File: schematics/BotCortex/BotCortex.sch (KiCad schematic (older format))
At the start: 60 parts, among them P1 2x Serial, P10 Stepper Upperarm, P11 Stepper Hip, P12 POWER_IN, P13 PowerEnableIn, P14 Power Stepper 2, P15 Power Stepper 3, P16 Power Stepper 4, P17 PowerEnableOut, P18 Power Stepper 5, P19 ODroid Power, P2 Herkulex Servo, P20 POTI 10K, P21 Reset_Conn, P22 Reset Conn, P23 LED-Driver-I2C, P24 UART6, P25 Thermal_Printer, P28 Power Stepper 1, P3 Encoder Socket 0, P4 Encoder Socket, P5 Stepper Elbow, P6 Power In uC Servo 9V, P7 Power Out uC Servo, P8 Stepper Forearm, P9 Stepper Wrist, Q1 BC237, Q2 BC237, SW2 reset, U1 7805, U2 LM7809ACT, U3 LM7809ACT, U4 Teensy_3.5, U5 7803

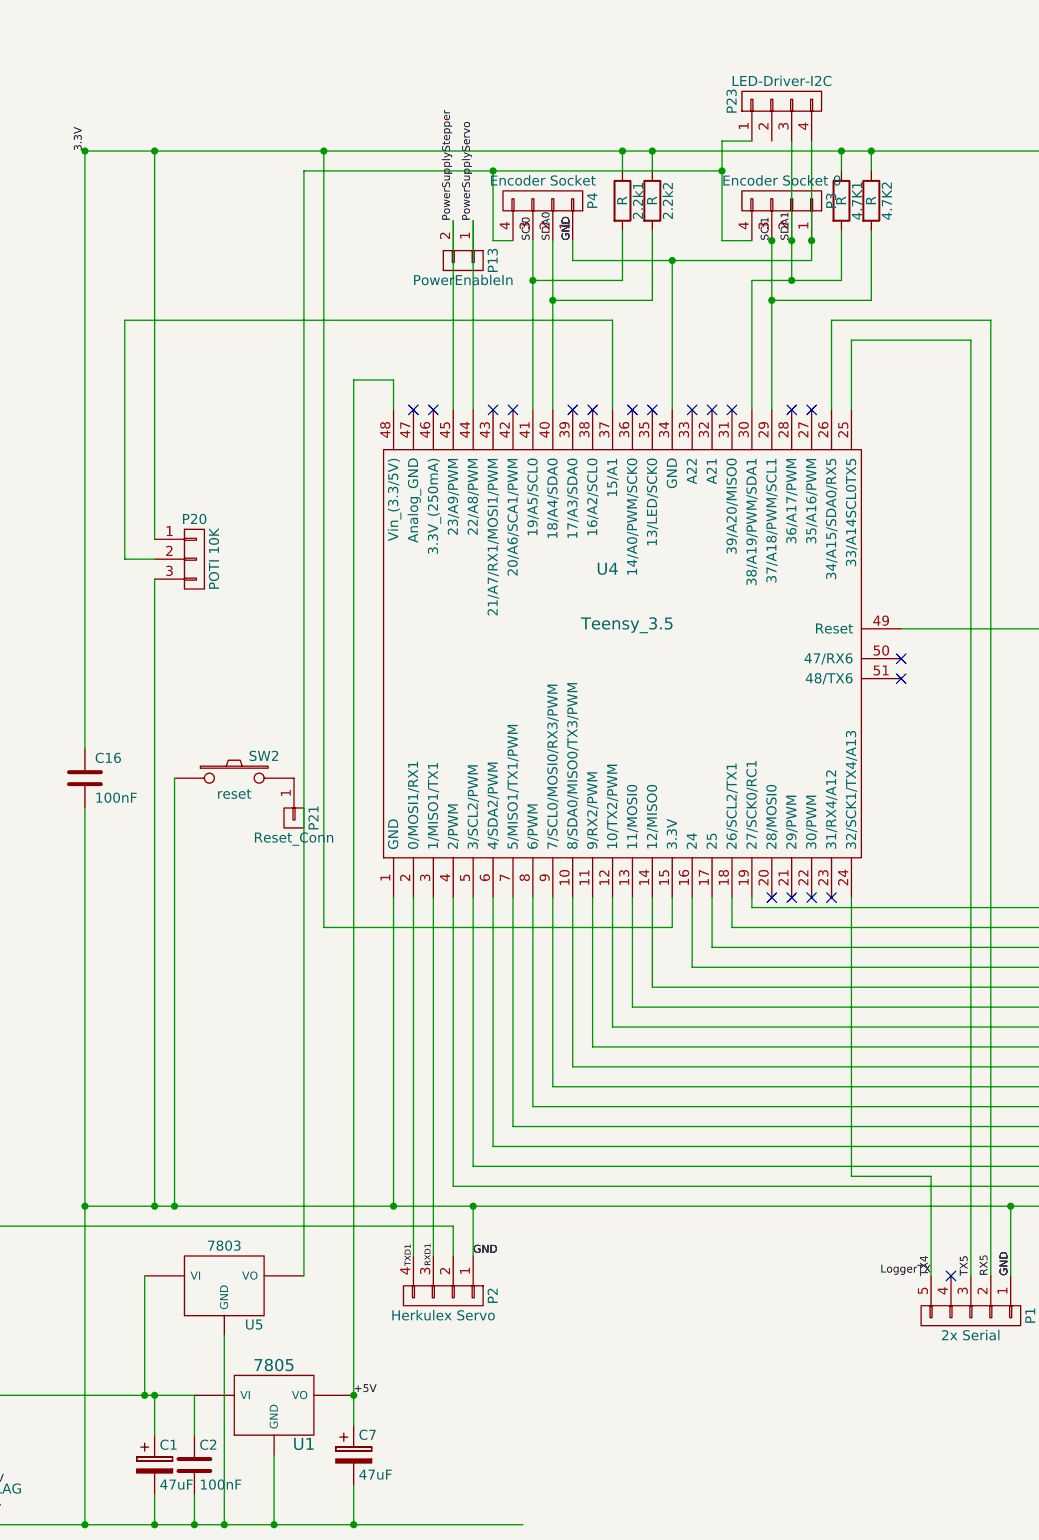
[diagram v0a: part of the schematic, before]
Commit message: encoder und stepper work with tinsy
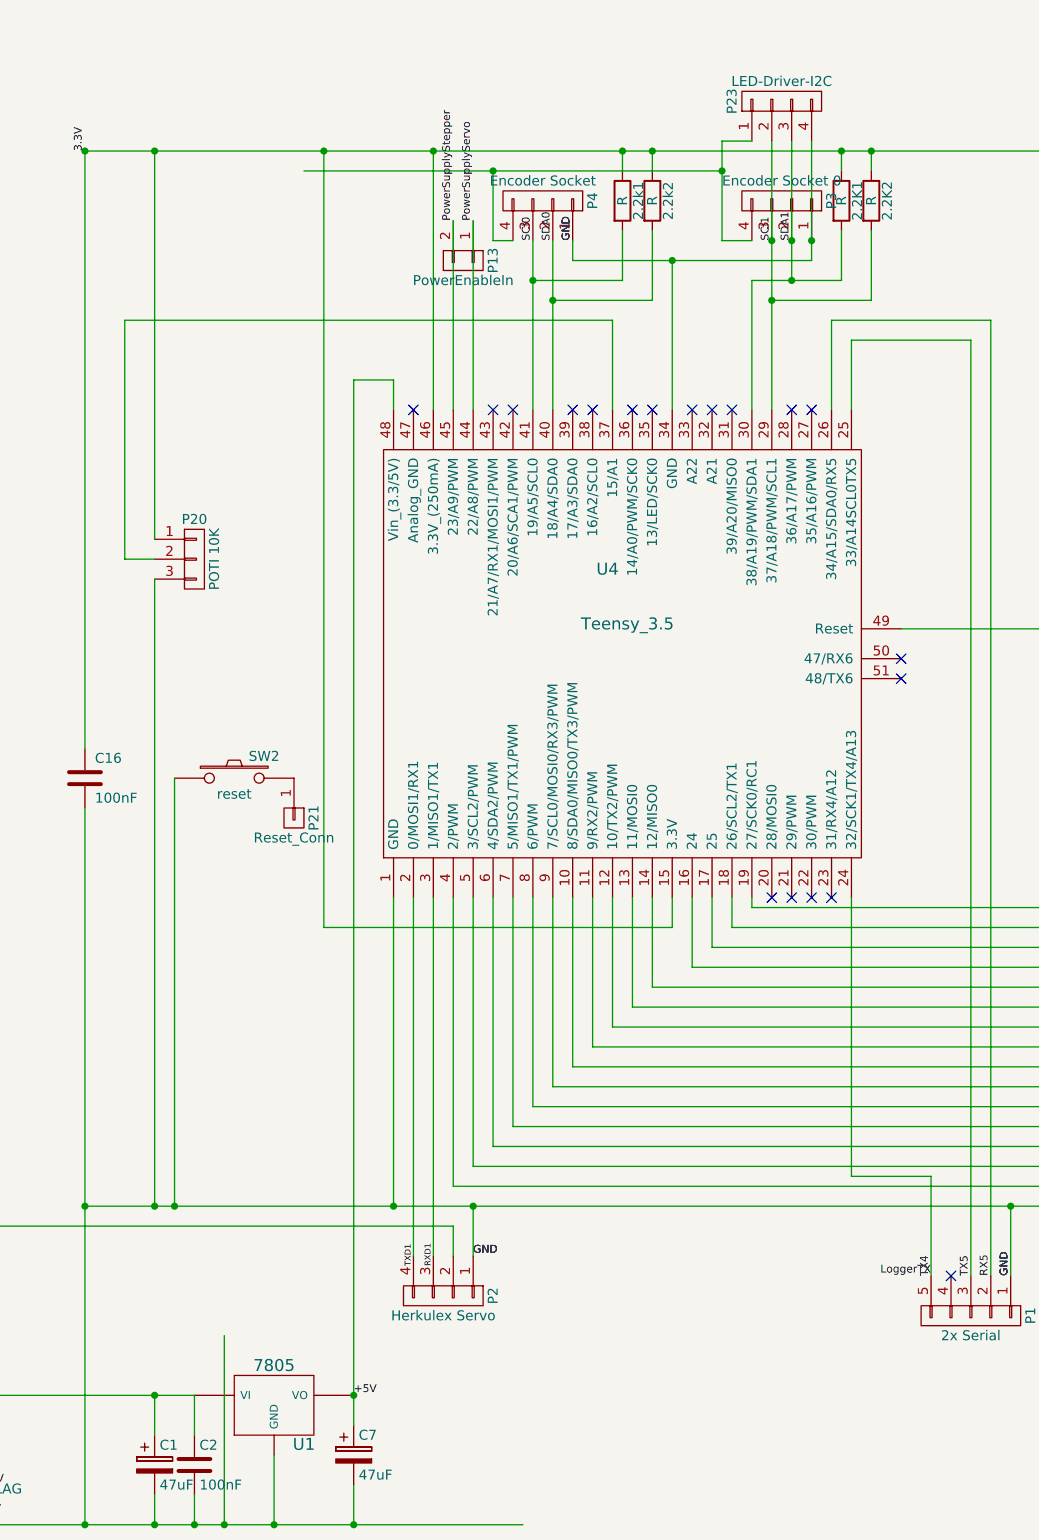
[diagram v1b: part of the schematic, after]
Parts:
- removed U5: 7803, BotCortex:78XX-TO-220, symbol 7805
- renumbered 4.7K1 to 2.2K1, 4.7K2 to 2.2K2
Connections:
- net 3.3V: now also U4.46 (3.3V_(250mA))
- net SCl1: now also P23.2 (P2)
- no-connect marks 24 -> 23
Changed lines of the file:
@@
 DIR4
 $Comp
-L GNDPWR #PWR01
+L GNDPWR #PWR2
 U 1 1 576CFF3F
 P 1200 7800
-F 0 "#PWR01" H 1200 7600 50  0001 C CNN
+F 0 "#PWR2" H 1200 7600 50  0001 C CNN
 F 1 "GNDPWR" H 1200 7670 50  0000 C CNN
 F 2 "" H 1200 7750 60  0000 C CNN
@@
 $EndComp
 $Comp
-L PWR_FLAG #FLG02
+L PWR_FLAG #FLG2
 U 1 1 576CF103
 P 1000 7150
-F 0 "#FLG02" H 1000 7245 50  0001 C CNN
+F 0 "#FLG2" H 1000 7245 50  0001 C CNN
 F 1 "PWR_FLAG" H 1000 7330 50  0000 C CNN
 F 2 "" H 1000 7150 60  0000 C CNN
@@
 $EndComp
 $Comp
-L GNDPWR #PWR03
+L GNDPWR #PWR1
 U 1 1 577CA6B0
 P 950 10800
-F 0 "#PWR03" H 950 10600 50  0001 C CNN
+F 0 "#PWR1" H 950 10600 50  0001 C CNN
 F 1 "GNDPWR" H 950 10670 50  0000 C CNN
 F 2 "" H 950 10750 60  0000 C CNN
@@
 $EndComp
 $Comp
-L PWR_FLAG #FLG04
+L PWR_FLAG #FLG1
 U 1 1 577CA6B1
 P 950 8600
-F 0 "#FLG04" H 950 8695 50  0001 C CNN
+F 0 "#FLG1" H 950 8695 50  0001 C CNN
 F 1 "PWR_FLAG" H 950 8780 50  0000 C CNN
 F 2 "" H 950 8600 60  0000 C CNN
@@
 $EndComp
 $Comp
-L PWR_FLAG #FLG05
+L PWR_FLAG #FLG3
 U 1 1 576D01C9
 P 1200 7800
-F 0 "#FLG05" H 1200 7895 50  0001 C CNN
+F 0 "#FLG3" H 1200 7895 50  0001 C CNN
 F 1 "PWR_FLAG" H 1200 7980 50  0000 C CNN
 F 2 "" H 1200 7800 60  0000 C CNN
@@
 $EndComp
 $Comp
-L R 4.7K1
+L R 2.2K1
 U 1 1 58590BCF
 P 5500 1150
-F 0 "4.7K1" V 5580 1150 50  0000 C CNN
+F 0 "2.2K1" V 5580 1150 50  0000 C CNN
 F 1 "R" V 5500 1150 50  0000 C CNN
 F 2 "Discret:R4" V 5430 1150 50  0001 C CNN
@@
 $EndComp
 $Comp
-L R 4.7K2
+L R 2.2K2
 U 1 1 58590D16
 P 5650 1150
-F 0 "4.7K2" V 5730 1150 50  0000 C CNN
+F 0 "2.2K2" V 5730 1150 50  0000 C CNN
 F 1 "R" V 5650 1150 50  0000 C CNN
 F 2 "Discret:R4" V 5580 1150 50  0001 C CNN
@@
 NoConn ~ 5150 4650
 NoConn ~ 3350 2200
-NoConn ~ 3450 2200
 NoConn ~ 3750 2200
 NoConn ~ 3850 2200
@@
 $EndComp
 $Comp
-L 7805 U5
-U 1 1 585B9A3D
-P 2400 6600
-F 0 "U5" H 2550 6404 50  0000 C CNN
-F 1 "7803" H 2400 6800 50  0000 C CNN
-F 2 "BotCortex:78XX-TO-220" H 2400 6600 50  0001 C CNN
-F 3 "" H 2400 6600 50  0000 C CNN
-	1    2400 6600
-	1    0    0    -1
-$EndComp
-$Comp
 L CONN_01X04 P3
 U 1 1 572B75C3
@@
 $EndComp
 $Comp
-L Teensy_3.5 U4
-U 1 1 585C33BC
-P 4500 3100
-F 0 "U4" H 4325 3200 60  0000 C CNN
-F 1 "Teensy_3.5" H 4425 2925 60  0000 C CNN
-F 2 "BotCortex:Teensy_3.5" H 4825 3025 60  0001 C CNN
-F 3 "" H 4825 3025 60  0000 C CNN
-	1    4500 3100
-	1    0    0    -1
-$EndComp
-$Comp
 L CONN_01X04 P25
 U 1 1 585C3FF4
@@
 Connection ~ 2400 7800
 Wire Wire Line
-	2000 6550 2000 7150
-Connection ~ 2000 7150
-Wire Wire Line
-	2800 6550 2800 1000
-Wire Wire Line
 	2800 1000 4900 1000
 Connection ~ 4900 1000
@@
 	5050 1550 5050 2200
 Wire Wire Line
-	5150 2200 5150 1350
+	5150 850  5150 2200
+$Comp
+L Teensy_3.5 U4
+U 1 1 585C33BC
+P 4500 3100
+F 0 "U4" H 4325 3200 60  0000 C CNN
+F 1 "Teensy_3.5" H 4425 2925 60  0000 C CNN
+F 2 "BotCortex:Teensy_3.5" H 4825 3025 60  0001 C CNN
+F 3 "" H 4825 3025 60  0000 C CNN
+	1    4500 3100
+	1    0    0    -1
+$EndComp
+Wire Wire Line
+	3450 2200 3450 900
+Connection ~ 3450 900
 $EndSCHEMATC
